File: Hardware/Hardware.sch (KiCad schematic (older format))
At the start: 27 parts

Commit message: Basic Done
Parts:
- added C14: 104, symbol C_Small
- added C15, C16: 105, symbol C_Small
- added P1, P2, P3, P4: CONN_01X01, symbol CONN_01X01
- added R5, R8: 0, symbol R_Small
- added R9: 4.7K, symbol R_Small
- added U3: MemoryLCD, symbol MemoryLCD
- gave numbers to parts that had none: 27
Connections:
- net OSCIN_32 is gone; now on net OSC32_IN: C9.1, Y2.1
- net SCL is gone; now on net IMU_SCL: R7.2, U4.23 (SCL)
- net SDA is gone; now on net IMU_SDA: R6.1, U4.24 (SDA)
- net +3V3: now also P1.1 (P1)
- net 3V3: now also C15.1, C16.1, R5.1, U3.6 (VDDA), U3.7 (VDD)
- net GND: now also C14.2, C15.2, C16.2, P2.1 (P1), R8.2, R9.2, U3.10 (VSSA), U3.9 (VSS)
- net LCD_COM: now reaches U2.13 (PA3/TIM2_CH4)
- net LCD_COM: now also U3.4 (EXTCOMIN)
- net LCD_SCLK: now reaches U2.15 (PA5/SPI1_SCK)
- net LCD_SCLK: now also U3.1 (SCLK)
- net LCD_SI: now reaches U2.17 (PA7/SPI1_MOSI)
- net LCD_SI: now also U3.2 (SI)
- net LCD_SCS: now reaches U2.18 (PB0)
- net LCD_SCS: now also U3.3 (SCS)
- net LCD_DISP: now reaches U2.19 (PB1)
- net LCD_DISP: now also C14.1, U3.5 (DISP)
- net IMU_SDA: now reaches U2.27 (PB14)
- net IMU_SCL: now reaches U2.28 (PB15)
- net USART_RX: now reaches U2.29 (PA8/USART1_RX)
- net USART_RX: now also P4.1 (P1)
- net USART_TX: now reaches U2.30 (PA9/USART1_TX)
- net USART_TX: now also P3.1 (P1)
- net AD0: no longer names the net of U4.9 (AD0)
- net AD0: now also R9.1
- net XCL: no longer names the net of U4.7 (AUX_CL)
- net XDA: no longer names the net of U4.6 (AUX_DA)
- new net MODE: R5.2, R8.1, U3.8 (EXTMODE)
- no-connect marks 4 -> 30

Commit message: Update Footprint
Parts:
- C1, C4: footprint (none) -> Capacitors_SMD:C_0805
- C10, C11, C12, C13, C14, C15, C16, C17, C18, C19, C2, C3, C5, C6, C7, C8, C9: footprint (none) -> Capacitors_SMD:C_0603
- P1, P2: footprint (none) -> Wire_Pads:SolderWirePad_single_0-8mmDrill
- P3, P4: footprint (none) -> Measurement_Points:Measurement_Point_Round-SMD-Pad_Small
- R1, R2, R3, R4, R5, R6, R7, R8, R9: footprint (none) -> Resistors_SMD:R_0603
- U1: footprint SOT-23 -> TO_SOT_Packages_SMD:SOT-23
- U2: footprint (none) -> Housings_DFN_QFN:UQFN-48-1EP_6x6mm_Pitch0.4mm
- U3: footprint (none) -> Connectors_Molex:AYF531
- U4: footprint (none) -> Housings_DFN_QFN:QFN-24-1EP_4x4mm_Pitch0.5mm
- Y1: footprint (none) -> Crystals:crystal_FA238-TSX3225
- Y2: footprint (none) -> Crystals:Crystal_Round_Vertical_2mm
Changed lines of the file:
@@
 F 0 "U2" H 5550 1800 60  0000 C CNN
 F 1 "stm32-LQFP64" H 6250 2000 60  0000 C CNN
-F 2 "" H 6100 3850 60  0000 C CNN
+F 2 "Housings_DFN_QFN:UQFN-48-1EP_6x6mm_Pitch0.4mm" H 6100 3850 60  0001 C CNN
 F 3 "" H 6100 3850 60  0000 C CNN
 	1    6250 3200
@@
 F 0 "U1" H 1500 850 50  0000 C CNN
 F 1 "APE8865N-33-HF-3" H 1750 1300 50  0000 C CNN
-F 2 "SOT-23" H 1750 1200 50  0000 C CIN
+F 2 "TO_SOT_Packages_SMD:SOT-23" H 1750 1200 50  0000 C CIN
 F 3 "" H 1750 1100 50  0000 C CNN
 	1    1750 1100
@@
 F 0 "C2" H 1210 1370 50  0000 L CNN
 F 1 "104" H 1210 1220 50  0000 L CNN
-F 2 "" H 1200 1300 50  0000 C CNN
+F 2 "Capacitors_SMD:C_0603" H 1200 1300 50  0001 C CNN
 F 3 "" H 1200 1300 50  0000 C CNN
 	1    1200 1300
@@
 F 0 "C3" H 2310 1370 50  0000 L CNN
 F 1 "104" H 2310 1220 50  0000 L CNN
-F 2 "" H 2300 1300 50  0000 C CNN
+F 2 "Capacitors_SMD:C_0603" H 2300 1300 50  0001 C CNN
 F 3 "" H 2300 1300 50  0000 C CNN
 	1    2300 1300
@@
 F 0 "C1" H 925 1400 50  0000 L CNN
 F 1 "106" H 925 1200 50  0000 L CNN
-F 2 "" H 938 1150 50  0000 C CNN
+F 2 "Capacitors_SMD:C_0805" H 938 1150 50  0001 C CNN
 F 3 "" H 900 1300 50  0000 C CNN
 	1    900  1300
@@
 F 0 "C4" H 2625 1400 50  0000 L CNN
 F 1 "106" H 2625 1200 50  0000 L CNN
-F 2 "" H 2638 1150 50  0000 C CNN
+F 2 "Capacitors_SMD:C_0805" H 2638 1150 50  0001 C CNN
 F 3 "" H 2600 1300 50  0000 C CNN
 	1    2600 1300
@@
 F 0 "C8" H 4860 2870 50  0000 L CNN
 F 1 "104" H 4860 2720 50  0000 L CNN
-F 2 "" H 4850 2800 50  0000 C CNN
+F 2 "Capacitors_SMD:C_0603" H 4850 2800 50  0001 C CNN
 F 3 "" H 4850 2800 50  0000 C CNN
 	1    4850 2800
@@
 F 0 "C13" H 4860 4470 50  0000 L CNN
 F 1 "104" H 4860 4320 50  0000 L CNN
-F 2 "" H 4850 4400 50  0000 C CNN
+F 2 "Capacitors_SMD:C_0603" H 4850 4400 50  0001 C CNN
 F 3 "" H 4850 4400 50  0000 C CNN
 	1    4850 4400
@@
 F 0 "C5" H 7510 2070 50  0000 L CNN
 F 1 "104" H 7510 1920 50  0000 L CNN
-F 2 "" H 7500 2000 50  0000 C CNN
+F 2 "Capacitors_SMD:C_0603" H 7500 2000 50  0001 C CNN
 F 3 "" H 7500 2000 50  0000 C CNN
 	1    7500 2000
@@
 F 0 "C11" H 7510 3370 50  0000 L CNN
 F 1 "104" H 7510 3220 50  0000 L CNN
-F 2 "" H 7500 3300 50  0000 C CNN
+F 2 "Capacitors_SMD:C_0603" H 7500 3300 50  0001 C CNN
 F 3 "" H 7500 3300 50  0000 C CNN
 	1    7500 3300
@@
 F 0 "R4" H 1430 2720 50  0000 L CNN
 F 1 "10K" H 1430 2660 50  0000 L CNN
-F 2 "" H 1400 2700 50  0000 C CNN
+F 2 "Resistors_SMD:R_0603" H 1400 2700 50  0001 C CNN
 F 3 "" H 1400 2700 50  0000 C CNN
 	1    1400 2700
@@
 F 0 "C10" H 1410 3170 50  0000 L CNN
 F 1 "104" H 1410 3020 50  0000 L CNN
-F 2 "" H 1400 3100 50  0000 C CNN
+F 2 "Capacitors_SMD:C_0603" H 1400 3100 50  0001 C CNN
 F 3 "" H 1400 3100 50  0000 C CNN
 	1    1400 3100
@@
 F 0 "C6" H 2710 2220 50  0000 L CNN
 F 1 "20pF" H 2710 2070 50  0000 L CNN
-F 2 "" H 2700 2150 50  0000 C CNN
+F 2 "Capacitors_SMD:C_0603" H 2700 2150 50  0001 C CNN
 F 3 "" H 2700 2150 50  0000 C CNN
 	1    2700 2150
@@
 F 0 "C7" H 2710 2720 50  0000 L CNN
 F 1 "20pF" H 2710 2570 50  0000 L CNN
-F 2 "" H 2700 2650 50  0000 C CNN
+F 2 "Capacitors_SMD:C_0603" H 2700 2650 50  0001 C CNN
 F 3 "" H 2700 2650 50  0000 C CNN
 	1    2700 2650
@@
 F 0 "R3" H 3230 2420 50  0000 L CNN
 F 1 "1M" H 3230 2360 50  0000 L CNN
-F 2 "" H 3200 2400 50  0000 C CNN
+F 2 "Resistors_SMD:R_0603" H 3200 2400 50  0001 C CNN
 F 3 "" H 3200 2400 50  0000 C CNN
 	1    3200 2400
@@
 F 0 "Y1" H 2950 2500 50  0000 C CNN
 F 1 "8MHz" H 2950 2300 50  0000 C CNN
-F 2 "" H 2950 2400 50  0000 C CNN
+F 2 "Crystals:crystal_FA238-TSX3225" H 2950 2400 50  0001 C CNN
 F 3 "" H 2950 2400 50  0000 C CNN
 	1    2950 2400
@@
 F 0 "C9" H 2710 3120 50  0000 L CNN
 F 1 "12pF" H 2710 2970 50  0000 L CNN
-F 2 "" H 2700 3050 50  0000 C CNN
+F 2 "Capacitors_SMD:C_0603" H 2700 3050 50  0001 C CNN
 F 3 "" H 2700 3050 50  0000 C CNN
 	1    2700 3050
@@
 F 0 "C12" H 2710 3620 50  0000 L CNN
 F 1 "12pF" H 2710 3470 50  0000 L CNN
-F 2 "" H 2700 3550 50  0000 C CNN
+F 2 "Capacitors_SMD:C_0603" H 2700 3550 50  0001 C CNN
 F 3 "" H 2700 3550 50  0000 C CNN
 	1    2700 3550
@@
 F 0 "Y2" H 3000 3400 50  0000 C CNN
 F 1 "32.768KHz" H 3000 3200 50  0000 C CNN
-F 2 "" H 3000 3300 50  0000 C CNN
+F 2 "Crystals:Crystal_Round_Vertical_2mm" H 3000 3300 50  0001 C CNN
 F 3 "" H 3000 3300 50  0000 C CNN
 	1    3000 3300
@@
 F 0 "R2" H 5730 1170 50  0000 L CNN
 F 1 "10K" H 5730 1110 50  0000 L CNN
-F 2 "" H 5700 1150 50  0000 C CNN
+F 2 "Resistors_SMD:R_0603" H 5700 1150 50  0001 C CNN
 F 3 "" H 5700 1150 50  0000 C CNN
 	1    5700 1150
@@
 F 0 "R1" H 5730 870 50  0000 L CNN
 F 1 "10K" H 5730 810 50  0000 L CNN
-F 2 "" H 5700 850 50  0000 C CNN
+F 2 "Resistors_SMD:R_0603" H 5700 850 50  0001 C CNN
 F 3 "" H 5700 850 50  0000 C CNN
 	1    5700 850
@@
 F 0 "U4" H 4250 6400 60  0000 C CNN
 F 1 "MPU6050" H 4250 5350 60  0000 C CNN
-F 2 "" H 4250 5900 60  0000 C CNN
+F 2 "Housings_DFN_QFN:QFN-24-1EP_4x4mm_Pitch0.5mm" H 4250 5900 60  0001 C CNN
 F 3 "" H 4250 5900 60  0000 C CNN
 	1    4250 5900
@@
 F 0 "C17" H 3210 5770 50  0000 L CNN
 F 1 "104" H 3210 5620 50  0000 L CNN
-F 2 "" H 3200 5700 50  0000 C CNN
+F 2 "Capacitors_SMD:C_0603" H 3200 5700 50  0001 C CNN
 F 3 "" H 3200 5700 50  0000 C CNN
 	1    3200 5700
@@
 F 0 "C19" H 3310 6120 50  0000 L CNN
 F 1 "104" H 3310 5970 50  0000 L CNN
-F 2 "" H 3300 6050 50  0000 C CNN
+F 2 "Capacitors_SMD:C_0603" H 3300 6050 50  0001 C CNN
 F 3 "" H 3300 6050 50  0000 C CNN
 	1    3300 6050
@@
 F 0 "R6" H 5030 5270 50  0000 L CNN
 F 1 "4.7K" H 5030 5210 50  0000 L CNN
-F 2 "" H 5000 5250 50  0000 C CNN
+F 2 "Resistors_SMD:R_0603" H 5000 5250 50  0001 C CNN
 F 3 "" H 5000 5250 50  0000 C CNN
 	1    5000 5250
@@
 F 0 "R7" H 5230 5270 50  0000 L CNN
 F 1 "4.7K" H 5230 5210 50  0000 L CNN
-F 2 "" H 5200 5250 50  0000 C CNN
+F 2 "Resistors_SMD:R_0603" H 5200 5250 50  0001 C CNN
 F 3 "" H 5200 5250 50  0000 C CNN
 	1    5200 5250
@@
 F 0 "C18" H 5060 6020 50  0000 L CNN
 F 1 "2200pF" H 5060 5870 50  0000 L CNN
-F 2 "" H 5050 5950 50  0000 C CNN
+F 2 "Capacitors_SMD:C_0603" H 5050 5950 50  0001 C CNN
 F 3 "" H 5050 5950 50  0000 C CNN
 	1    5050 5950
@@
 F 0 "R9" H 3530 5970 50  0000 L CNN
 F 1 "4.7K" H 3530 5910 50  0000 L CNN
-F 2 "" H 3500 5950 50  0000 C CNN
+F 2 "Resistors_SMD:R_0603" H 3500 5950 50  0001 C CNN
 F 3 "" H 3500 5950 50  0000 C CNN
 	1    3500 5950
@@
 F 0 "C14" H 7360 5670 50  0000 L CNN
 F 1 "104" H 7360 5520 50  0000 L CNN
-F 2 "" H 7350 5600 50  0000 C CNN
+F 2 "Capacitors_SMD:C_0603" H 7350 5600 50  0001 C CNN
 F 3 "" H 7350 5600 50  0000 C CNN
 	1    7350 5600
@@
 F 0 "C16" H 8010 5670 50  0000 L CNN
 F 1 "105" H 8010 5520 50  0000 L CNN
-F 2 "" H 8000 5600 50  0000 C CNN
+F 2 "Capacitors_SMD:C_0603" H 8000 5600 50  0001 C CNN
 F 3 "" H 8000 5600 50  0000 C CNN
 	1    8000 5600
@@
 F 0 "C15" H 7710 5670 50  0000 L CNN
 F 1 "105" H 7710 5520 50  0000 L CNN
-F 2 "" H 7700 5600 50  0000 C CNN
+F 2 "Capacitors_SMD:C_0603" H 7700 5600 50  0001 C CNN
 F 3 "" H 7700 5600 50  0000 C CNN
 	1    7700 5600
@@
 F 0 "R5" H 9830 4970 50  0000 L CNN
 F 1 "0" H 9830 4910 50  0000 L CNN
-F 2 "" H 9800 4950 50  0000 C CNN
+F 2 "Resistors_SMD:R_0603" H 9800 4950 50  0001 C CNN
 F 3 "" H 9800 4950 50  0000 C CNN
 	1    9800 4950
@@
 F 0 "R8" H 9830 5270 50  0000 L CNN
 F 1 "0" H 9830 5210 50  0000 L CNN
-F 2 "" H 9800 5250 50  0000 C CNN
+F 2 "Resistors_SMD:R_0603" H 9800 5250 50  0001 C CNN
 F 3 "" H 9800 5250 50  0000 C CNN
 	1    9800 5250
@@
 F 0 "P1" H 650 1150 50  0000 C CNN
 F 1 "CONN_01X01" V 750 1050 50  0000 C CNN
-F 2 "" H 650 1050 50  0000 C CNN
+F 2 "Wire_Pads:SolderWirePad_single_0-8mmDrill" H 650 1050 50  0001 C CNN
 F 3 "" H 650 1050 50  0000 C CNN
 	1    650  1050
@@
 F 0 "P2" H 650 1650 50  0000 C CNN
 F 1 "CONN_01X01" V 750 1550 50  0000 C CNN
-F 2 "" H 650 1550 50  0000 C CNN
+F 2 "Wire_Pads:SolderWirePad_single_0-8mmDrill" H 650 1550 50  0001 C CNN
 F 3 "" H 650 1550 50  0000 C CNN
 	1    650  1550
@@
 F 0 "P3" H 8900 3650 50  0000 C CNN
 F 1 "CONN_01X01" V 9000 3550 50  0000 C CNN
-F 2 "" H 8900 3550 50  0000 C CNN
+F 2 "Measurement_Points:Measurement_Point_Round-SMD-Pad_Small" H 8900 3550 50  0001 C CNN
 F 3 "" H 8900 3550 50  0000 C CNN
 	1    8900 3550
@@
 F 0 "P4" H 8900 4300 50  0000 C CNN
 F 1 "CONN_01X01" V 9000 4200 50  0000 C CNN
-F 2 "" H 8900 4200 50  0000 C CNN
+F 2 "Measurement_Points:Measurement_Point_Round-SMD-Pad_Small" H 8900 4200 50  0001 C CNN
 F 3 "" H 8900 4200 50  0000 C CNN
 	1    8900 4200
@@
 F 0 "U3" H 8800 5950 60  0000 C CNN
 F 1 "MemoryLCD" H 8800 4700 60  0000 C CNN
-F 2 "" H 8250 5350 60  0000 C CNN
+F 2 "Connectors_Molex:AYF531" H 8250 5350 60  0001 C CNN
 F 3 "" H 8250 5350 60  0000 C CNN
 	1    8800 5350

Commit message: PCB Layout Done And Add Gerber Files
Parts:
- U2: footprint Housings_DFN_QFN:UQFN-48-1EP_6x6mm_Pitch0.4mm -> Housings_DFN_QFN:QFN-48-1EP_7x7mm_Pitch0.5mm
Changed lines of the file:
@@
 F 0 "U2" H 5550 1800 60  0000 C CNN
 F 1 "stm32-LQFP64" H 6250 2000 60  0000 C CNN
-F 2 "Housings_DFN_QFN:UQFN-48-1EP_6x6mm_Pitch0.4mm" H 6100 3850 60  0001 C CNN
+F 2 "Housings_DFN_QFN:QFN-48-1EP_7x7mm_Pitch0.5mm" H 6100 3850 60  0001 C CNN
 F 3 "" H 6100 3850 60  0000 C CNN
 	1    6250 3200

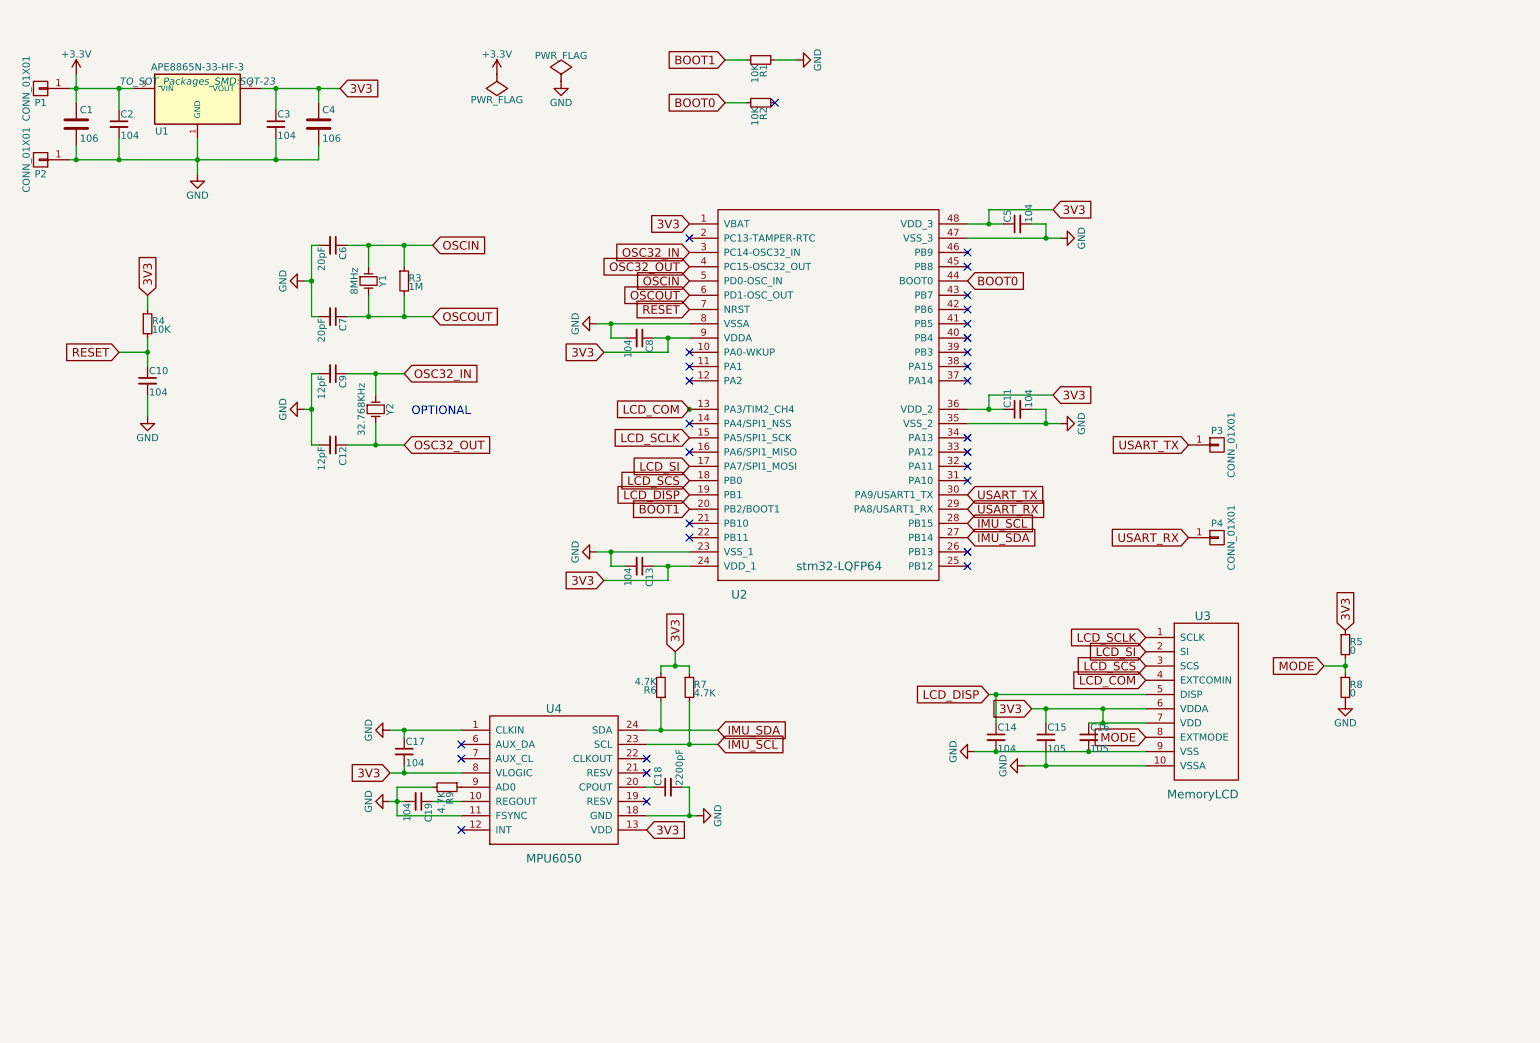
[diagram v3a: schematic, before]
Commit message: feat: (4 Layer)
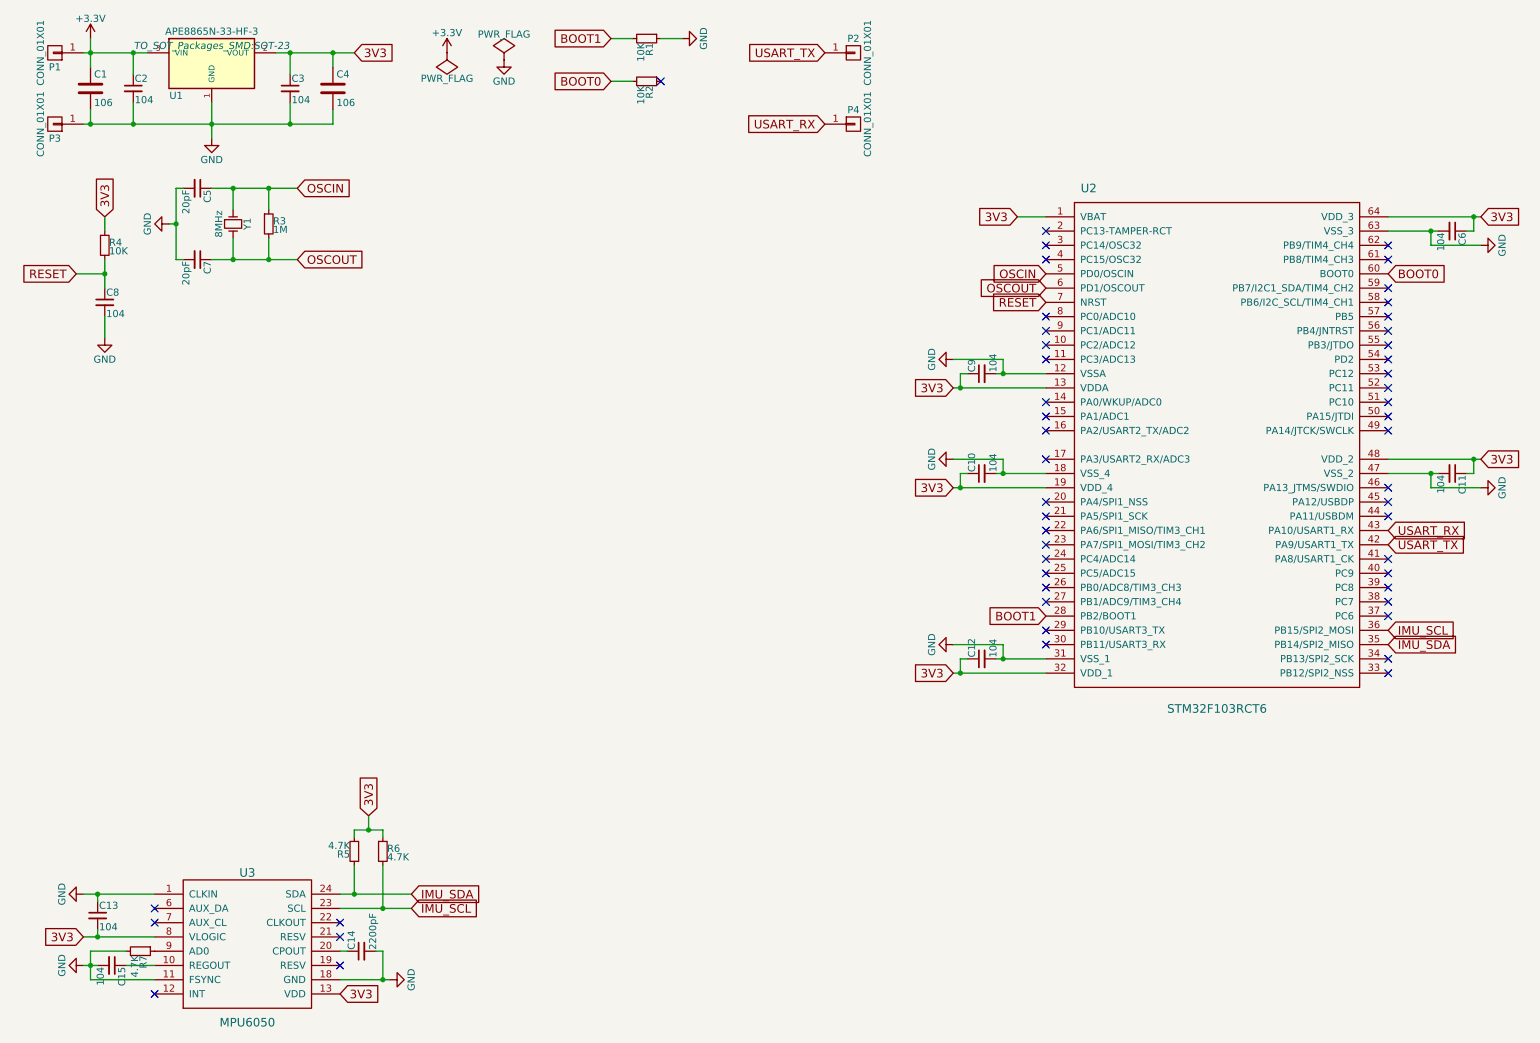
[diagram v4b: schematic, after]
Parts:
- removed C13, C14, C5, C8: 104, Capacitors_SMD:C_0603, symbol C_Small
- removed C15, C16: 105, Capacitors_SMD:C_0603, symbol C_Small
- removed R5, R8: 0, Resistors_SMD:R_0603, symbol R_Small
- removed U2: stm32-LQFP64, Housings_DFN_QFN:QFN-48-1EP_7x7mm_Pitch0.5mm, symbol stm32-LQFP64
- removed U3: MemoryLCD, Connectors_Molex:AYF531, symbol MemoryLCD
- removed Y2: 32.768KHz, Crystals:Crystal_Round_Vertical_2mm, symbol Crystal_Small
- added C10, C6: 104, Capacitors_SMD:C_0603, symbol C_Small
- added U2: STM32F103RCT6, Housings_QFP:LQFP-64_10x10mm_Pitch0.5mm, symbol STM32F103RCT6
- C1, C4: footprint Capacitors_SMD:C_0805 -> Capacitors_SMD:C_0603
- C12, C9: value 12pF -> 104
- Y1: footprint Crystals:crystal_FA238-TSX3225 -> Crystals:SMD-5032
- renumbered C17 to C13, C18 to C14, C19 to C15, C6 to C5, C10 to C8, P3 to P2, P2 to P3, R6 to R5, R7 to R6, R9 to R7, U4 to U3
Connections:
- net OSC32_IN is gone; now on net 3V3: C9.1
- net OSC32_OUT is gone; now on net 3V3: C12.1
- net 3V3: now also C10.1, C6.1, U2.1 (VBAT), U2.13 (VDDA), U2.19 (VDD_4), U2.32 (VDD_1), U2.48 (VDD_2), U2.64 (VDD_3)
- net BOOT0: now also U2.60 (BOOT0)
- net BOOT1: now also U2.28 (PB2/BOOT1)
- net GND: now also C10.2, C6.2, U2.12 (VSSA), U2.18 (VSS_4), U2.31 (VSS_1), U2.47 (VSS_2), U2.63 (VSS_3)
- net IMU_SCL: now also U2.36 (PB15/SPI2_MOSI)
- net IMU_SDA: now also U2.35 (PB14/SPI2_MISO)
- net OSCIN: now also U2.5 (PD0/OSCIN)
- net OSCOUT: now also U2.6 (PD1/OSCOUT)
- net RESET: now also U2.7 (NRST)
- net USART_RX: now also U2.43 (PA10/USART1_RX)
- net USART_TX: now also U2.42 (PA9/USART1_TX)
- no-connect marks 30 -> 51
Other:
- note removed: "OPTIONAL\n"
- moved on the sheet: C1, C13, C14, C15, C2, C3, C4, C5, C7, C8, P1, P2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
